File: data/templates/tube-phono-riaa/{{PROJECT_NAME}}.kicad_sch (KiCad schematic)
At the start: 20 parts, among them X1 12AX7, X2 12AX7

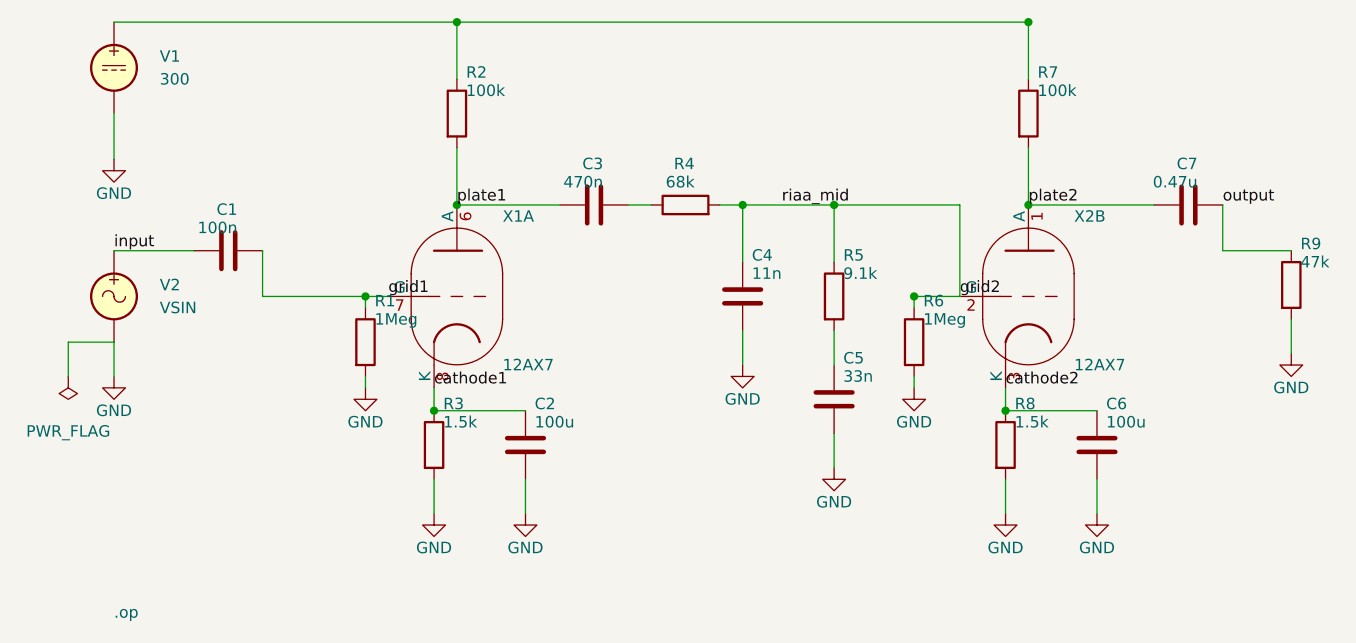
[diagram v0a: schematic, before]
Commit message: T187 Phase 1: domain + facade snap-on-write entry-point
Domain (src/domain/grid.py):
- snap_to_grid(value, grid_mm=1.27) pure function; idempotent, FP-stable
- GridStepMm semantic alias
- OffGridEndpoint / OffGridReport frozen pydantic VO
- OffGridPositionError for EFACTORY_STRICT_GRID=1 strict mode

Facade (adapters/outbound/schematic_kicad/facade.py):
- _to_position now snaps both tuple-input and Position-input (idempotent
  for already-on-grid). Catches the edge-case where builder constructs
  Position(x_mm=..., y_mm=...) directly with off-grid coords (e.g. wire
  endpoint in bjt-ce-nfb at y=96.19 — root cause of disconnect after
  snap moved R_E to y=96.52).
- connect() snaps its Position start/end via _to_position too. Manhattan
  corner inherits snapped coords.
- _snap_position helper: silent snap by default; EFACTORY_STRICT_GRID=1
  raises OffGridPositionError for real off-grid drift (>1e-6 mm), FP
  jitter always silently snapped.
- name param plumbed through all add_* / junction / no_connect / label
  / spice_directive callsites for diagnostic error messages.
- add_ground / add_pwr_flag restructured to resolve reference before
  _to_position (so error carries real ref, not '<unknown>').

Templates regenerated (8 buildered via existing _BAKERS):
- se-amp, nfb-se-amp, op-amp-inverting, bjt-ce-nfb, tube-pp-amp,
  tube-line-preamp, tube-phono-riaa, active-lpf-sallen-key
- ERC check: 0 endpoint_off_grid warnings, 0 errors for all 8.
- 3 T031 builderless templates (6p13s/6zh32p/6zh38p) still dirty;
  fixed in Phase 4 via reverse-engineered builder.

Tests:
- New tests/unit/domain/test_grid.py (20 cases): snap correctness +
  idempotence + FP-jitter + custom grid + frozen VO + strict-mode error.
- New T187 cases in test_schematic_facade.py: silent snap default,
  strict-mode raise, FP-jitter tolerance, label/spice/ground/pwr_flag
  snap paths.
- Updated existing tests with off-grid literal coords (100→101.6,
  50→50.8 etc.) to articulate the new on-grid invariant.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
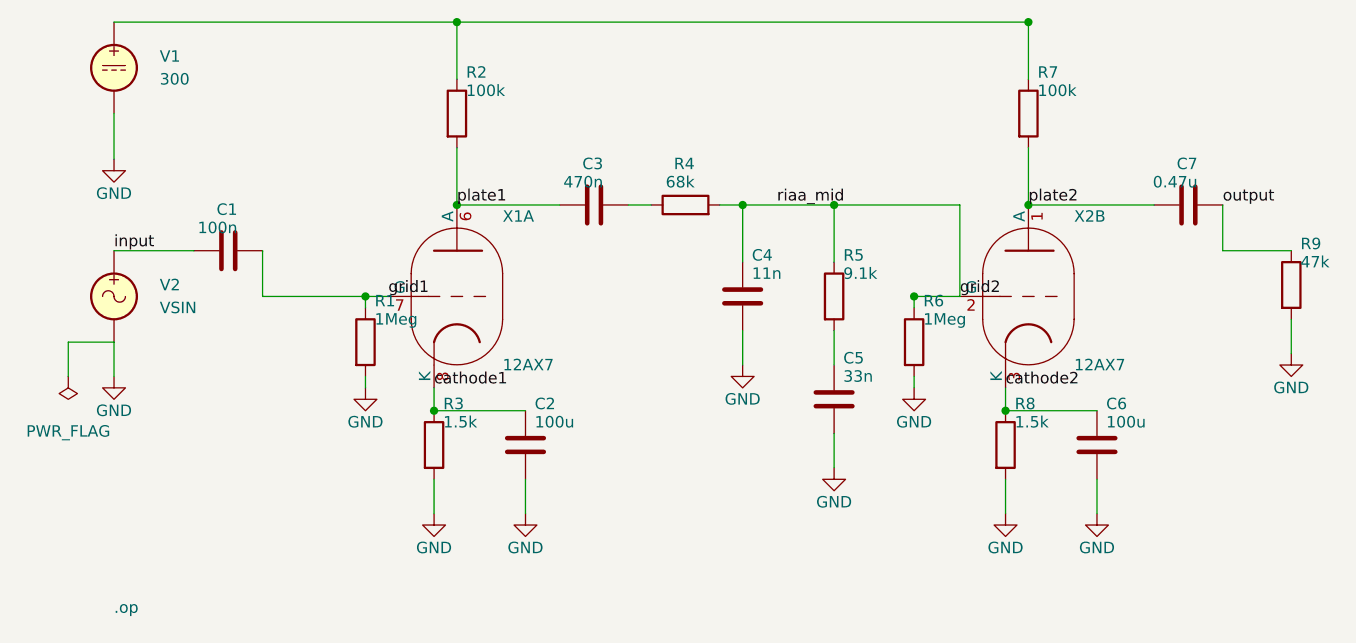
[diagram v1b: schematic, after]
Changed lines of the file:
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@@
 	)
 	(label "riaa_mid"
-		(at 125 78.74 0)
+		(at 124.46 78.74 0)
 		(effects
 			(font
@@
 	(text ".op"
 		(exclude_from_sim no)
-		(at 50.8 125 0)
+		(at 50.8 124.46 0)
 		(effects
 			(font
